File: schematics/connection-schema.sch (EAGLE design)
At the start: 23 parts

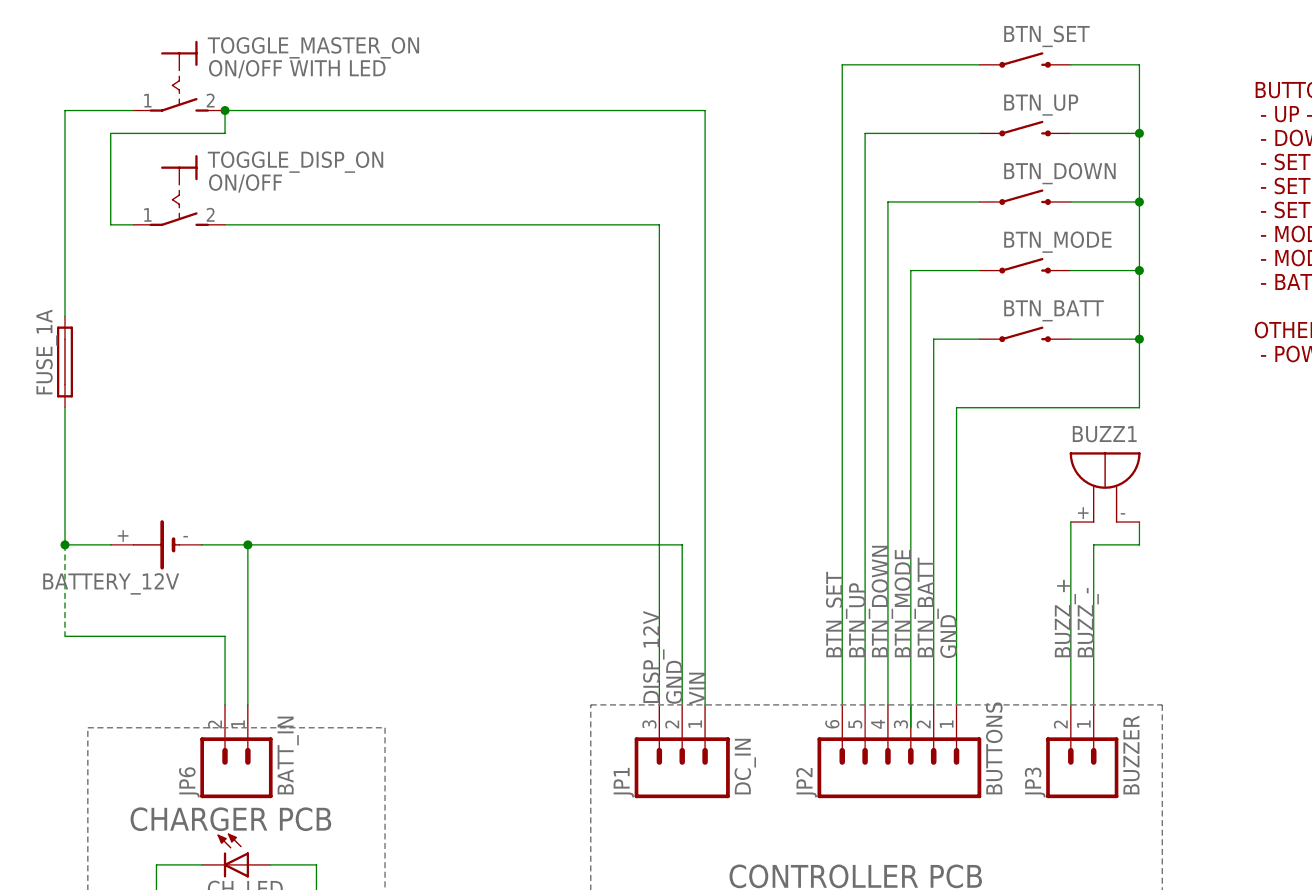
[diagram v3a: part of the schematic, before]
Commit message: schematics: add different assembly variants, small fixes
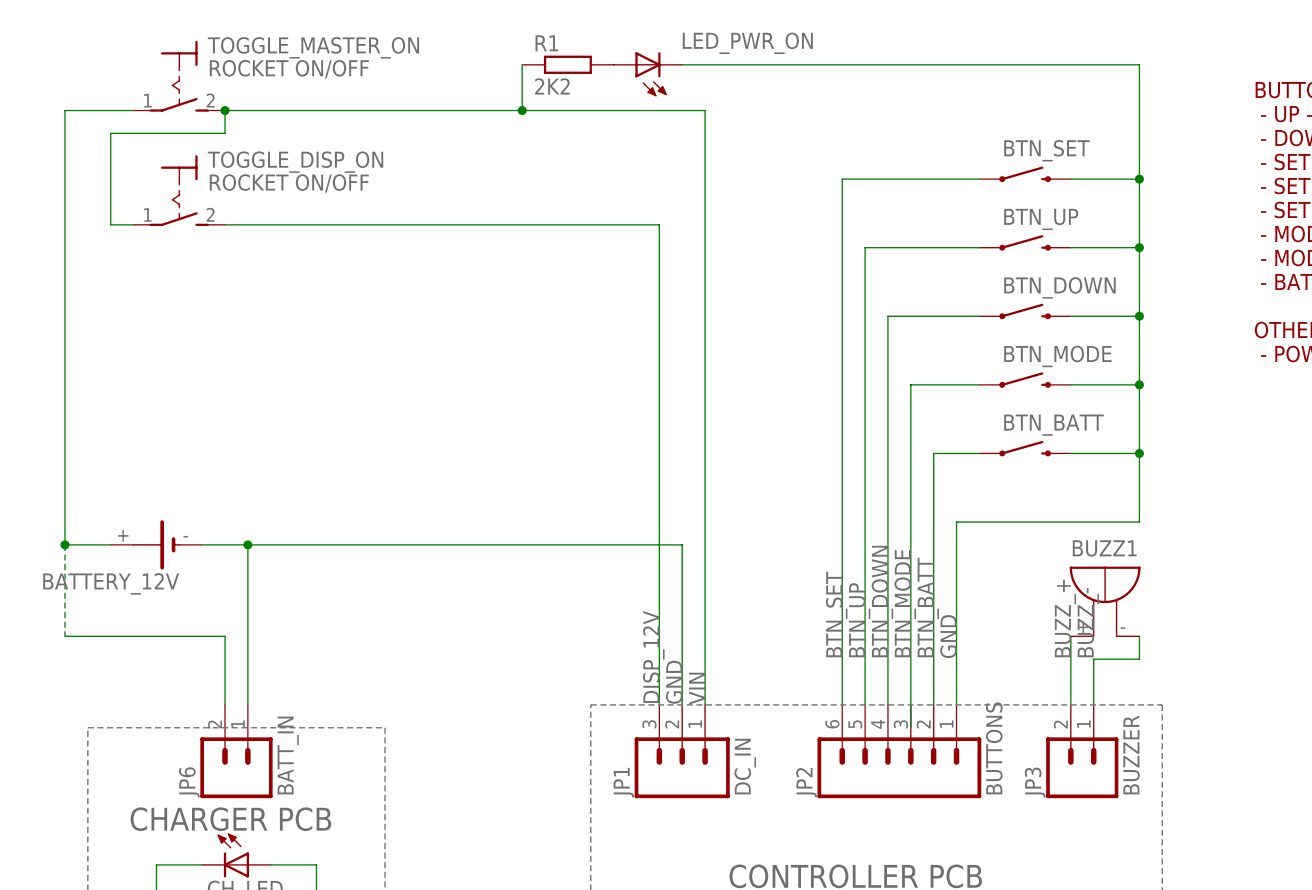
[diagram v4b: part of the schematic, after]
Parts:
- removed FUSE_1A: FUSEKS9V, fuse:FUSEKS9V
- added LED_PWR_ON: (no value), led:LED5MM
- added R1: 2K2, resistor:R-EU_0207_10
- TOGGLE_DISP_ON: value ON/OFF -> ROCKET ON/OFF
- TOGGLE_MASTER_ON: value ON/OFF WITH LED -> ROCKET ON/OFF
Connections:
- removed net N$5: FUSE_1A.2, TOGGLE_MASTER_ON.P
- new net N$2: LED_PWR_ON.A, R1.2
- net GND: now also LED_PWR_ON.C
- net N$1: now also TOGGLE_MASTER_ON.P; no longer FUSE_1A.1
- net VIN: now also R1.1
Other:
- moved on the sheet: BTN_BATT, BTN_DOWN, BTN_MODE, BTN_SET, BTN_UP, BUZZ1
